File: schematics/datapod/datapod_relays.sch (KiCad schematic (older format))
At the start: 11 parts, among them J1 Conn_01x02, J2 Conn_02x03_Odd_Even, J3 Conn_01x02, K1 DS2E-SL2-DC5V, K2 DS2E-SL2-DC5V, Q1 FDG1024NZ, Q2 FDG1024NZ

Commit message: improved pcb outline
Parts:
- K1, K2: Part# 255-1066-ND -> ED11086-ND; Part#-2 (none) -> 255-1066-ND
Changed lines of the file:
@@
 F 4 "Digikey" H 2200 2450 50  0001 C CNN "Vendor"
 F 5 "ED11086-ND" H 2200 2450 50  0001 C CNN "Part#"
-F 6 "255-1066-ND" H 2200 2450 50  0001 C CNN "Part#"
+F 6 "255-1066-ND" H 2200 2450 50  0001 C CNN "Part#-2"
 	1    2200 2450
 	1    0    0    -1
@@
 F 4 "Digikey" H 6550 2450 50  0001 C CNN "Vendor"
 F 5 "ED11086-ND" H 6550 2450 50  0001 C CNN "Part#"
-F 6 "255-1066-ND" H 6550 2450 50  0001 C CNN "Part#"
+F 6 "255-1066-ND" H 6550 2450 50  0001 C CNN "Part#-2"
 	1    6550 2450
 	1    0    0    -1

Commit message: fixed bad gnd trace on 3.3v circuit and added comments to the silkscreen
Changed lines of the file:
@@
 Wire Wire Line
 	1850 3000 1150 3000
-Wire Wire Line
-	1150 3000 1150 2700
 $Comp
 L power:GND #PWR012
@@
 	1    0    0    -1
 $EndComp
+Wire Wire Line
+	1150 2700 1150 3000
 $EndSCHEMATC

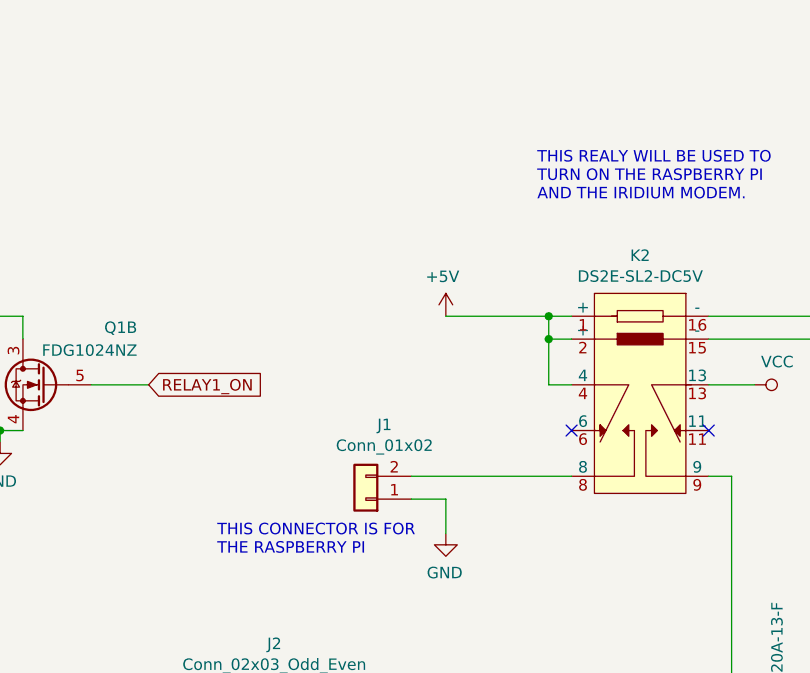
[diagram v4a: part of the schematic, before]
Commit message: added a jumper to select between 5v and 14v for the raspberry pi
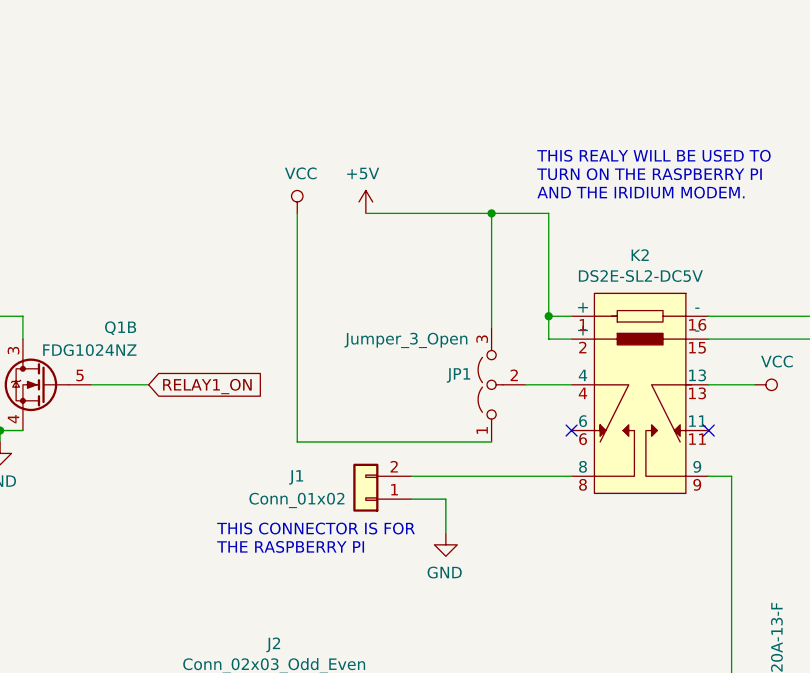
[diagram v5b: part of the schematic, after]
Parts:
- added JP1: Jumper_3_Open, Jumper:SolderJumper-3_P1.3mm_Open_RoundedPad1.0x1.5mm, symbol Jumper:Jumper_3_Open
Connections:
- net +5V: now also JP1.3 (B); no longer K2.4
- net VCC: now also JP1.1 (A)
- new net: JP1.2 (C), K2.4
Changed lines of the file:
@@
 Wire Wire Line
 	6200 2800 6100 2800
-Wire Wire Line
-	6100 2800 6100 2700
-Connection ~ 6100 2700
 Text Notes 4150 1300 0    50   ~ 0
 THE RELAYS ARE IN A RESET CONDITION WHEN THE\nCOIL ON PINS 2 & 15 IS ACTIVATED. iN A RESET CONDITION\n4 & 6 ARE SHORTED AND 13 &11 ARE SHORTED.\n\nWHEN THE COIL ON PINS 1 & 16 IS ACTIVATED THEN PINS 4 & 8 ARE\nSHORTED AND PINS 13 & 9 ARE SHORTED.
@@
 L power:+5V #PWR011
 U 1 1 5DC3B83B
-P 5650 2700
-F 0 "#PWR011" H 5650 2550 50  0001 C CNN
-F 1 "+5V" H 5665 2873 50  0000 C CNN
-F 2 "" H 5650 2700 50  0001 C CNN
-F 3 "" H 5650 2700 50  0001 C CNN
-	1    5650 2700
+P 5300 2250
+F 0 "#PWR011" H 5300 2100 50  0001 C CNN
+F 1 "+5V" H 5315 2423 50  0000 C CNN
+F 2 "" H 5300 2250 50  0001 C CNN
+F 3 "" H 5300 2250 50  0001 C CNN
+	1    5300 2250
 	-1   0    0    -1
 $EndComp
-Wire Wire Line
-	5650 2700 6100 2700
-Wire Wire Line
-	6200 3000 6100 3000
-Wire Wire Line
-	6100 3000 6100 2800
-Connection ~ 6100 2800
 $Comp
 L power:VCC #PWR?
@@
 U 1 1 5DC79621
 P 5300 3500
-F 0 "J1" H 5218 3175 50  0000 C CNN
-F 1 "Conn_01x02" H 5218 3266 50  0000 C CNN
+F 0 "J1" H 5600 3400 50  0000 C CNN
+F 1 "Conn_01x02" H 5600 3500 50  0000 C CNN
 F 2 "Connector_Molex:Molex_Mini-Fit_Jr_5569-02A1_2x01_P4.20mm_Horizontal" H 5300 3500 50  0001 C CNN
 F 3 "https://www.molex.com/pdm_docs/sd/039291028_sd.pdf" H 5300 3500 50  0001 C CNN
@@
 Text Notes 4650 3750 0    50   ~ 0
 THIS CONNECTOR IS FOR \nTHE RASPBERRY PI
+Wire Wire Line
+	1150 2700 1150 3000
+Wire Wire Line
+	6100 2800 6100 2700
 $Comp
 L Relays_user_made:DS2E-SL2-DC5V K2
@@
 $EndComp
 Wire Wire Line
-	1150 2700 1150 3000
+	6200 3000 6000 3000
+Wire Wire Line
+	6100 2700 6100 2250
+Wire Wire Line
+	6100 2250 5850 2250
+Connection ~ 6100 2700
+$Comp
+L power:VCC #PWR?
+U 1 1 5E2EAE48
+P 5000 2250
+AR Path="/5E423883/5E2EAE48" Ref="#PWR?"  Part="1"
+AR Path="/5E14D46E/5E2EAE48" Ref="#PWR0112"  Part="1"
+F 0 "#PWR0112" H 5000 2100 50  0001 C CNN
+F 1 "VCC" H 5017 2423 50  0000 C CNN
+F 2 "" H 5000 2250 50  0001 C CNN
+F 3 "" H 5000 2250 50  0001 C CNN
+	1    5000 2250
+	1    0    0    -1
+$EndComp
+$Comp
+L Jumper:Jumper_3_Open JP1
+U 1 1 5E2F0090
+P 5850 3000
+F 0 "JP1" V 5896 3087 50  0000 L CNN
+F 1 "Jumper_3_Open" V 6050 3100 50  0000 L CNN
+F 2 "Jumper:SolderJumper-3_P1.3mm_Open_RoundedPad1.0x1.5mm" H 5850 3000 50  0001 C CNN
+F 3 "~" H 5850 3000 50  0001 C CNN
+	1    5850 3000
+	0    -1   -1   0
+$EndComp
+Wire Wire Line
+	5850 2750 5850 2250
+Connection ~ 5850 2250
+Wire Wire Line
+	5850 2250 5300 2250
+Wire Wire Line
+	5850 3250 5000 3250
+Wire Wire Line
+	5000 3250 5000 2250
 $EndSCHEMATC

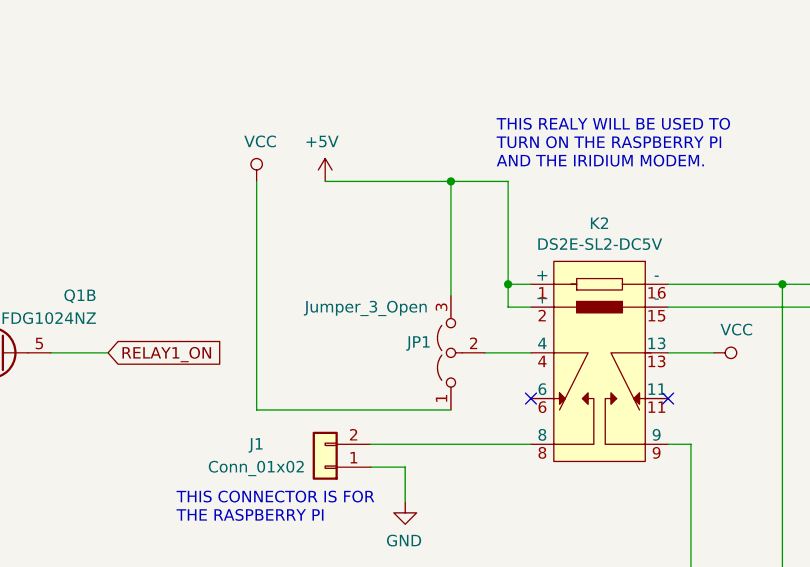
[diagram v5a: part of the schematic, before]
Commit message: added rtc stuff , rotated db9s , added on/off transistors for max chip and sdcard
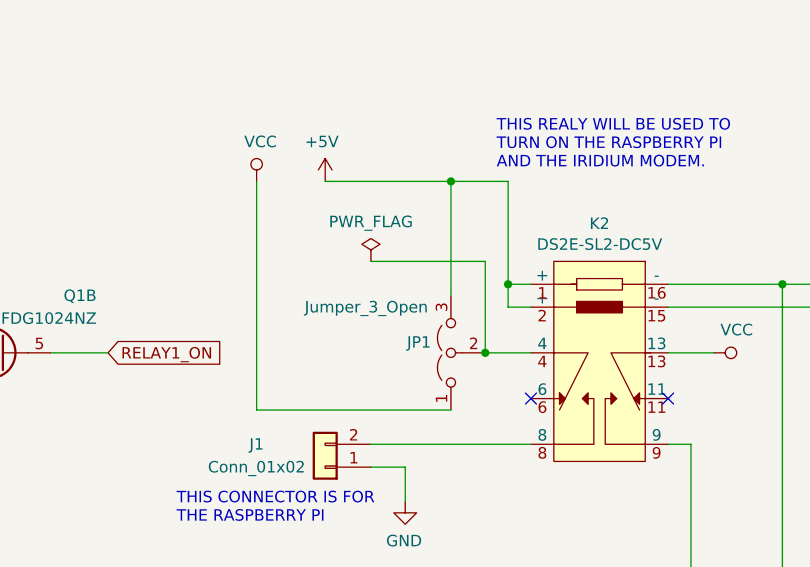
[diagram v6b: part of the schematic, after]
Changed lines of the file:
@@
 Wire Wire Line
 	5000 3250 5000 2250
+$Comp
+L power:PWR_FLAG #FLG0103
+U 1 1 5E2C0274
+P 5500 2600
+F 0 "#FLG0103" H 5500 2675 50  0001 C CNN
+F 1 "PWR_FLAG" H 5500 2773 50  0000 C CNN
+F 2 "" H 5500 2600 50  0001 C CNN
+F 3 "~" H 5500 2600 50  0001 C CNN
+	1    5500 2600
+	1    0    0    -1
+$EndComp
+Wire Wire Line
+	5500 2600 6000 2600
+Wire Wire Line
+	6000 2600 6000 3000
+Connection ~ 6000 3000
 $EndSCHEMATC

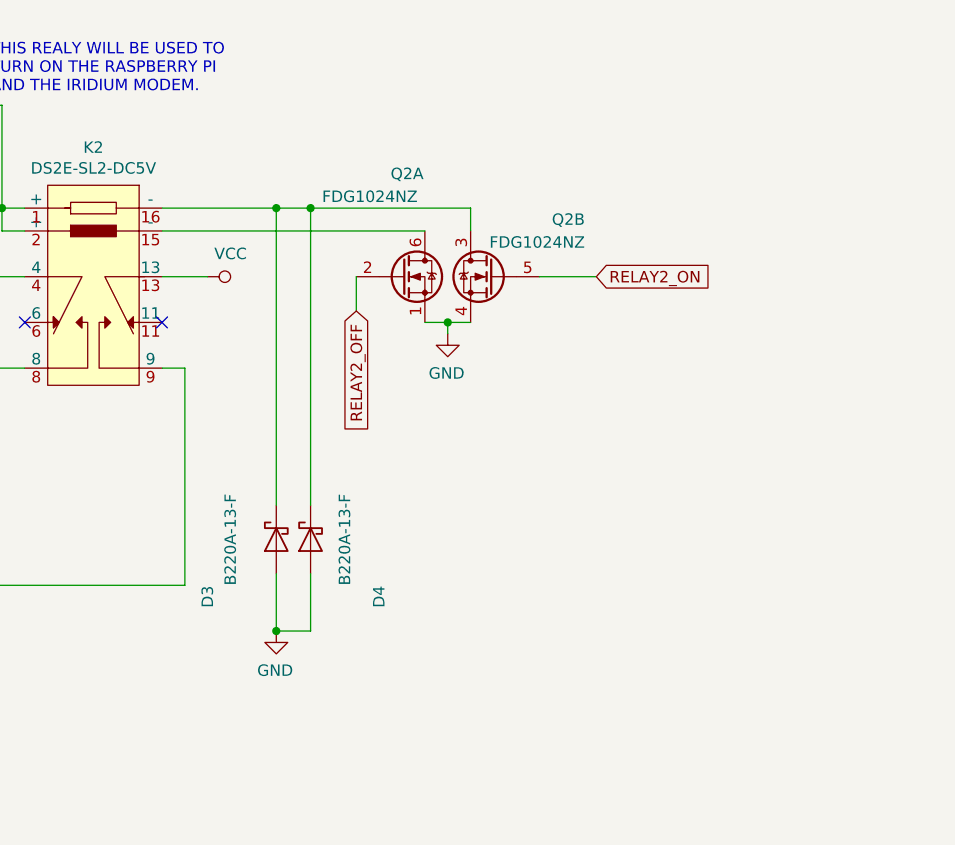
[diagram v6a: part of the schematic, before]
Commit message: rev 3 , moved db9 connectors out and added ajumper to change output to 14.4v
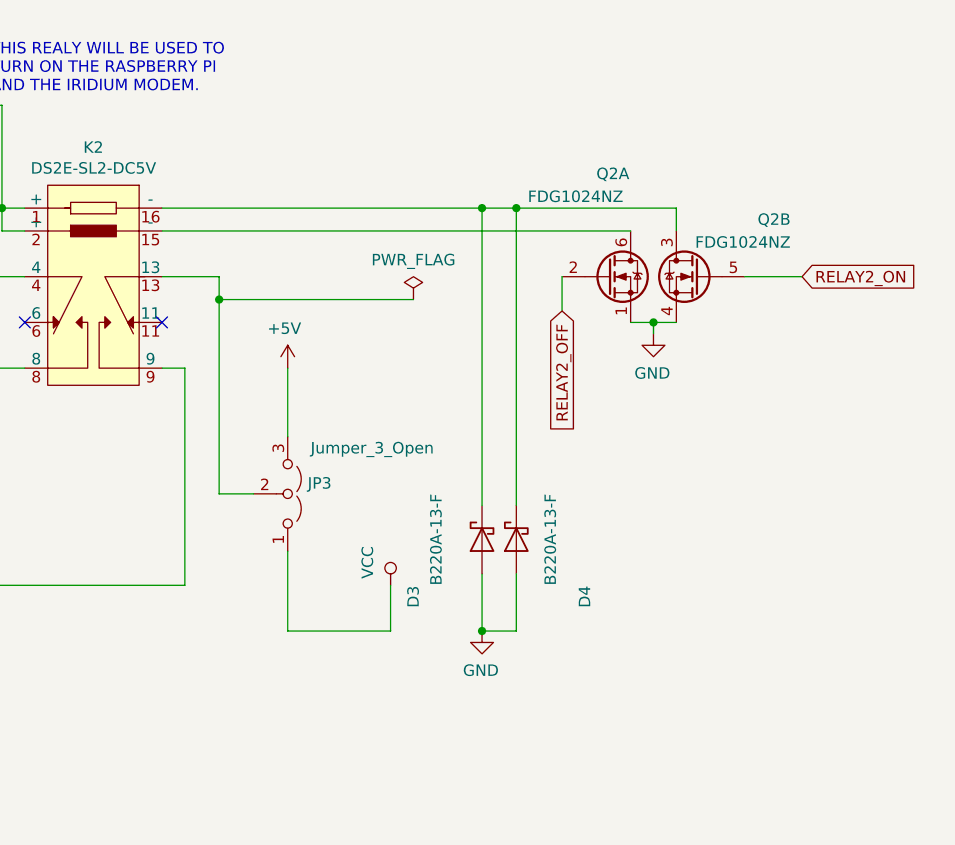
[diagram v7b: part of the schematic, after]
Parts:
- added JP3: Jumper_3_Open, Jumper:SolderJumper-3_P1.3mm_Open_RoundedPad1.0x1.5mm, symbol Jumper:Jumper_3_Open
- JP1: Part# (none) -> DNI
- K1, K2: footprint Package_DIP:DIP-16_W7.62mm_SMDSocket_SmallPads -> Package_DIP:DIP-16_W8.89mm_SMDSocket_LongPads
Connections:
- net +5V: now also JP3.3 (B)
- net VCC: now also JP3.1 (A); no longer K2.13
- new net: JP3.2 (C), K2.13
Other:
- moved on the sheet: D3, D4, Q2A, Q2B
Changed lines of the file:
@@
 Text GLabel 3300 3150 3    50   Input ~ 0
 RELAY1_OFF
-Text GLabel 7650 3150 3    50   Input ~ 0
+Text GLabel 8550 3150 3    50   Input ~ 0
 RELAY2_OFF
 Wire Wire Line
-	8700 3000 8450 3000
-Text GLabel 8700 3000 2    50   Input ~ 0
+	9600 3000 9350 3000
+Text GLabel 9600 3000 2    50   Input ~ 0
 RELAY2_ON
 Wire Wire Line
-	7650 3000 7650 3150
-Wire Wire Line
-	8150 2700 8150 2800
-Wire Wire Line
-	8150 3200 8050 3200
-Wire Wire Line
-	8050 3200 7950 3200
-Wire Wire Line
-	8050 3250 8050 3200
-Connection ~ 8050 3200
+	8550 3000 8550 3150
+Wire Wire Line
+	9050 2700 9050 2800
+Wire Wire Line
+	9050 3200 8950 3200
+Wire Wire Line
+	8950 3200 8850 3200
+Wire Wire Line
+	8950 3250 8950 3200
+Connection ~ 8950 3200
 $Comp
 L power:GND #PWR015
 U 1 1 5E1668DE
-P 8050 3250
-F 0 "#PWR015" H 8050 3000 50  0001 C CNN
-F 1 "GND" H 8055 3077 50  0000 C CNN
-F 2 "" H 8050 3250 50  0001 C CNN
-F 3 "" H 8050 3250 50  0001 C CNN
-	1    8050 3250
+P 8950 3250
+F 0 "#PWR015" H 8950 3000 50  0001 C CNN
+F 1 "GND" H 8955 3077 50  0000 C CNN
+F 2 "" H 8950 3250 50  0001 C CNN
+F 3 "" H 8950 3250 50  0001 C CNN
+	1    8950 3250
 	-1   0    0    -1
 $EndComp
@@
 L Transistor_FET:FDG1024NZ Q2
 U 1 1 5E1668D8
-P 7850 3000
-F 0 "Q2" H 7800 3450 50  0000 L CNN
-F 1 "FDG1024NZ" H 7500 3350 50  0000 L CNN
-F 2 "Package_TO_SOT_SMD:SOT-363_SC-70-6" H 8050 2925 50  0001 L CIN
-F 3 "http://www.fairchildsemi.com/ds/FD/FDG1024NZ.pdf" H 7850 3000 50  0001 L CNN
-F 4 "Digikey" H 7850 3000 50  0001 C CNN "Vendor"
-F 5 "FDG1024NZFSCT-ND" H 7850 3000 50  0001 C CNN "Part#"
-	1    7850 3000
+P 8750 3000
+F 0 "Q2" H 8700 3450 50  0000 L CNN
+F 1 "FDG1024NZ" H 8400 3350 50  0000 L CNN
+F 2 "Package_TO_SOT_SMD:SOT-363_SC-70-6" H 8950 2925 50  0001 L CIN
+F 3 "http://www.fairchildsemi.com/ds/FD/FDG1024NZ.pdf" H 8750 3000 50  0001 L CNN
+F 4 "Digikey" H 8750 3000 50  0001 C CNN "Vendor"
+F 5 "FDG1024NZFSCT-ND" H 8750 3000 50  0001 C CNN "Part#"
+	1    8750 3000
 	1    0    0    -1
 $EndComp
@@
 L Transistor_FET:FDG1024NZ Q2
 U 2 1 5E1668D0
-P 8250 3000
-F 0 "Q2" H 7850 3250 50  0000 L CNN
-F 1 "FDG1024NZ" H 7850 3150 50  0000 L CNN
-F 2 "Package_TO_SOT_SMD:SOT-363_SC-70-6" H 8450 2925 50  0001 L CIN
-F 3 "http://www.fairchildsemi.com/ds/FD/FDG1024NZ.pdf" H 8250 3000 50  0001 L CNN
-F 4 "Digikey" H 8250 3000 50  0001 C CNN "Vendor"
-F 5 "FDG1024NZFSCT-ND" H 8250 3000 50  0001 C CNN "Part#"
-	2    8250 3000
+P 9150 3000
+F 0 "Q2" H 8750 3250 50  0000 L CNN
+F 1 "FDG1024NZ" H 8750 3150 50  0000 L CNN
+F 2 "Package_TO_SOT_SMD:SOT-363_SC-70-6" H 9350 2925 50  0001 L CIN
+F 3 "http://www.fairchildsemi.com/ds/FD/FDG1024NZ.pdf" H 9150 3000 50  0001 L CNN
+F 4 "Digikey" H 9150 3000 50  0001 C CNN "Vendor"
+F 5 "FDG1024NZFSCT-ND" H 9150 3000 50  0001 C CNN "Part#"
+	2    9150 3000
 	-1   0    0    -1
 $EndComp
@@
 	3600 2800 2950 2800
 Wire Wire Line
-	8150 2700 7450 2700
-Wire Wire Line
-	7950 2800 6800 2800
+	9050 2700 8350 2700
 $Comp
 L Diode:B220 D?
 U 1 1 5E2EB42E
-P 7300 4150
+P 8200 4150
 AR Path="/5E2EB42E" Ref="D?"  Part="1"
 AR Path="/5E14D46E/5E2EB42E" Ref="D3"  Part="1"
-F 0 "D3" H 7550 4450 50  0000 C CNN
-F 1 "B220A-13-F " H 7300 4350 50  0000 C CNN
-F 2 "Diode_SMD:D_SMA" H 7300 3975 50  0001 C CNN
-F 3 "http://www.jameco.com/Jameco/Products/ProdDS/1538777.pdf" H 7300 4150 50  0001 C CNN
-F 4 "Digikey" H 7300 4150 50  0001 C CNN "Vendor"
-F 5 "B220A-FDIDKR-ND" H 7300 4150 50  0001 C CNN "Part#"
-	1    7300 4150
+F 0 "D3" H 8450 4450 50  0000 C CNN
+F 1 "B220A-13-F " H 8200 4350 50  0000 C CNN
+F 2 "Diode_SMD:D_SMA" H 8200 3975 50  0001 C CNN
+F 3 "http://www.jameco.com/Jameco/Products/ProdDS/1538777.pdf" H 8200 4150 50  0001 C CNN
+F 4 "Digikey" H 8200 4150 50  0001 C CNN "Vendor"
+F 5 "B220A-FDIDKR-ND" H 8200 4150 50  0001 C CNN "Part#"
+	1    8200 4150
 	0    -1   1    0
 $EndComp
@@
 L Diode:B220 D?
 U 1 1 5E2EB435
-P 7450 4150
+P 8350 4150
 AR Path="/5E2EB435" Ref="D?"  Part="1"
 AR Path="/5E14D46E/5E2EB435" Ref="D4"  Part="1"
-F 0 "D4" H 7700 3850 50  0000 C CNN
-F 1 "B220A-13-F " H 7450 4000 50  0000 C CNN
-F 2 "Diode_SMD:D_SMA" H 7450 3975 50  0001 C CNN
-F 3 "http://www.jameco.com/Jameco/Products/ProdDS/1538777.pdf" H 7450 4150 50  0001 C CNN
-F 4 "Digikey" H 7450 4150 50  0001 C CNN "Vendor"
-F 5 "B220A-FDIDKR-ND" H 7450 4150 50  0001 C CNN "Part#"
-	1    7450 4150
+F 0 "D4" H 8600 3850 50  0000 C CNN
+F 1 "B220A-13-F " H 8350 4000 50  0000 C CNN
+F 2 "Diode_SMD:D_SMA" H 8350 3975 50  0001 C CNN
+F 3 "http://www.jameco.com/Jameco/Products/ProdDS/1538777.pdf" H 8350 4150 50  0001 C CNN
+F 4 "Digikey" H 8350 4150 50  0001 C CNN "Vendor"
+F 5 "B220A-FDIDKR-ND" H 8350 4150 50  0001 C CNN "Part#"
+	1    8350 4150
 	0    -1   1    0
 $EndComp
@@
 	2950 2800 2450 2800
 Wire Wire Line
-	7450 4000 7450 2700
-Connection ~ 7450 2700
-Wire Wire Line
-	7450 2700 7300 2700
-Wire Wire Line
-	7300 4000 7300 2700
-Connection ~ 7300 2700
-Wire Wire Line
-	7300 2700 6800 2700
+	8350 4000 8350 2700
+Connection ~ 8350 2700
+Wire Wire Line
+	8350 2700 8200 2700
+Wire Wire Line
+	8200 4000 8200 2700
+Connection ~ 8200 2700
 $Comp
 L power:GND #PWR017
@@
 L power:GND #PWR019
 U 1 1 5E2FD2F8
-P 7300 4550
-F 0 "#PWR019" H 7300 4300 50  0001 C CNN
-F 1 "GND" H 7305 4377 50  0000 C CNN
-F 2 "" H 7300 4550 50  0001 C CNN
-F 3 "" H 7300 4550 50  0001 C CNN
-	1    7300 4550
+P 8200 4550
+F 0 "#PWR019" H 8200 4300 50  0001 C CNN
+F 1 "GND" H 8205 4377 50  0000 C CNN
+F 2 "" H 8200 4550 50  0001 C CNN
+F 3 "" H 8200 4550 50  0001 C CNN
+	1    8200 4550
 	-1   0    0    -1
 $EndComp
@@
 	3100 4500 2950 4500
 Wire Wire Line
-	7450 4300 7450 4550
-Wire Wire Line
-	7450 4550 7300 4550
+	8350 4300 8350 4550
+Wire Wire Line
+	8350 4550 8200 4550
 Connection ~ 2950 4500
 Wire Wire Line
-	7300 4300 7300 4550
-Connection ~ 7300 4550
+	8200 4300 8200 4550
+Connection ~ 8200 4550
 Wire Wire Line
 	3100 4250 3100 4500
@@
 F 0 "K1" H 2150 2465 50  0000 C CNN
 F 1 "DS2E-SL2-DC5V" H 2150 2374 50  0000 C CNN
-F 2 "Package_DIP:DIP-16_W7.62mm_SMDSocket_SmallPads" H 2200 2500 50  0001 C CNN
+F 2 "Package_DIP:DIP-16_W8.89mm_SMDSocket_LongPads" H 2200 2500 50  0001 C CNN
 F 3 "https://www3.panasonic.biz/ac/e_download/control/relay/signal/catalog/mech_eng_ds.pdf" H 2200 2500 50  0001 C CNN
 F 4 "Digikey" H 2200 2450 50  0001 C CNN "Vendor"
@@
 L power:VCC #PWR?
 U 1 1 5DC41A5A
-P 7000 3000
+P 7800 4350
 AR Path="/5E423883/5DC41A5A" Ref="#PWR?"  Part="1"
 AR Path="/5E14D46E/5DC41A5A" Ref="#PWR013"  Part="1"
-F 0 "#PWR013" H 7000 2850 50  0001 C CNN
-F 1 "VCC" V 6900 3100 50  0000 C CNN
-F 2 "" H 7000 3000 50  0001 C CNN
-F 3 "" H 7000 3000 50  0001 C CNN
-	1    7000 3000
-	0    1    1    0
-$EndComp
-Wire Wire Line
-	6800 3000 7000 3000
+F 0 "#PWR013" H 7800 4200 50  0001 C CNN
+F 1 "VCC" V 7700 4450 50  0000 C CNN
+F 2 "" H 7800 4350 50  0001 C CNN
+F 3 "" H 7800 4350 50  0001 C CNN
+	1    7800 4350
+	1    0    0    -1
+$EndComp
 $Comp
 L Connector_Generic:Conn_02x03_Top_Bottom J2
@@
 F 0 "K2" H 6500 2465 50  0000 C CNN
 F 1 "DS2E-SL2-DC5V" H 6500 2374 50  0000 C CNN
-F 2 "Package_DIP:DIP-16_W7.62mm_SMDSocket_SmallPads" H 6550 2500 50  0001 C CNN
+F 2 "Package_DIP:DIP-16_W8.89mm_SMDSocket_LongPads" H 6550 2500 50  0001 C CNN
 F 3 "https://www3.panasonic.biz/ac/e_download/control/relay/signal/catalog/mech_eng_ds.pdf" H 6550 2500 50  0001 C CNN
 F 4 "Digikey" H 6550 2450 50  0001 C CNN "Vendor"
@@
 F 2 "Jumper:SolderJumper-3_P1.3mm_Open_RoundedPad1.0x1.5mm" H 5850 3000 50  0001 C CNN
 F 3 "~" H 5850 3000 50  0001 C CNN
+F 4 "DNI" V 5850 3000 50  0001 C CNN "Part#"
 	1    5850 3000
 	0    -1   -1   0
@@
 	6000 2600 6000 3000
 Connection ~ 6000 3000
+Wire Wire Line
+	6800 2700 8200 2700
+Wire Wire Line
+	6800 2800 8850 2800
+$Comp
+L Jumper:Jumper_3_Open JP3
+U 1 1 5E3D2741
+P 7350 3950
+F 0 "JP3" V 7396 4037 50  0000 L CNN
+F 1 "Jumper_3_Open" V 7550 4050 50  0000 L CNN
+F 2 "Jumper:SolderJumper-3_P1.3mm_Open_RoundedPad1.0x1.5mm" H 7350 3950 50  0001 C CNN
+F 3 "~" H 7350 3950 50  0001 C CNN
+F 4 "DNI" V 7350 3950 50  0001 C CNN "Part#"
+	1    7350 3950
+	0    1    -1   0
+$EndComp
+Wire Wire Line
+	7350 4200 7350 4550
+Wire Wire Line
+	7350 4550 7800 4550
+Wire Wire Line
+	7800 4550 7800 4350
+Wire Wire Line
+	6800 3000 7050 3000
+Wire Wire Line
+	7050 3000 7050 3100
+Wire Wire Line
+	7050 3950 7200 3950
+$Comp
+L power:+5V #PWR06
+U 1 1 5E3EDA90
+P 7350 3400
+F 0 "#PWR06" H 7350 3250 50  0001 C CNN
+F 1 "+5V" H 7365 3573 50  0000 C CNN
+F 2 "" H 7350 3400 50  0001 C CNN
+F 3 "" H 7350 3400 50  0001 C CNN
+	1    7350 3400
+	-1   0    0    -1
+$EndComp
+Wire Wire Line
+	7350 3400 7350 3700
+$Comp
+L power:PWR_FLAG #FLG0102
+U 1 1 5E3F15B2
+P 7900 3100
+F 0 "#FLG0102" H 7900 3175 50  0001 C CNN
+F 1 "PWR_FLAG" H 7900 3273 50  0000 C CNN
+F 2 "" H 7900 3100 50  0001 C CNN
+F 3 "~" H 7900 3100 50  0001 C CNN
+	1    7900 3100
+	1    0    0    -1
+$EndComp
+Wire Wire Line
+	7900 3100 7050 3100
+Connection ~ 7050 3100
+Wire Wire Line
+	7050 3100 7050 3950
 $EndSCHEMATC
